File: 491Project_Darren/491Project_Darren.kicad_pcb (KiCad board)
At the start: 4 copper layers, 77 x 77 mm, 1 part, among them U2 Pico

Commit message: PCB
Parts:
- added C1: 100nF, 491_Footprints:CAP_805_CER, F.Cu at (142.5, 158.0)
- added C10: 100nF, 491_Footprints:CAP_805_CER, F.Cu at (148.5, 187.5)
- added C11: 10uF, 491_Footprints:CAP_ALUM, F.Cu at (127.0, 110.5)
- added C12: 10uF, 491_Footprints:CAP_ALUM, F.Cu at (154.0, 185.0)
- added C2: 100nF, 491_Footprints:CAP_805_CER, F.Cu at (124.5, 104.5)
- added C3: 10uF, 491_Footprints:CAP_ALUM, F.Cu at (154.9, 159.0)
- added C4: 0.1uF, 491_Footprints:CAP_CER_0.1uF_1206, F.Cu at (130.0, 194.0)
- added C5: 1000pF, 491_Footprints:CAP_805_CER, F.Cu at (129.9, 190.0)
- added C6: 1nF, 491_Footprints:CAP_805_CER, F.Cu at (129.9, 187.5)
- added C7: 22nF, 491_Footprints:CAP_805_CER, F.Cu at (129.5, 181.0)
- added C8: 100nF, 491_Footprints:CAP_805_CER, F.Cu at (139.5, 153.0)
- added C9: 100nF, 491_Footprints:CAP_805_CER, F.Cu at (119.9, 103.5)
- added J1: RJ45, 491_Footprints:RJ45_Amphenol_RJHSE5380, F.Cu at (116.0, 73.1)
- added J2: RJ45, 491_Footprints:RJ45_Amphenol_RJHSE5380, F.Cu at (175.3, 77.0)
- added R1: 110, 491_Footprints:R_805, F.Cu at (124.4, 88.5)
- added R10: 1k, 491_Footprints:R_805, F.Cu at (70.4, 89.8)
- added R11: 1k, 491_Footprints:R_805, F.Cu at (111.4, 153.0)
- added R12: 1k, 491_Footprints:R_805, F.Cu at (120.5, 96.5)
- added R13: 1k, 491_Footprints:R_805, F.Cu at (162.4, 159.0)
- added R14: 1k, 491_Footprints:R_805, F.Cu at (149.6, 164.0)
- added R15: 1k, 491_Footprints:R_805, F.Cu at (153.0, 191.6)
- added R16: 47k, 491_Footprints:R_805, F.Cu at (148.9, 192.0)
- added R17: 1k, 491_Footprints:R_805, F.Cu at (121.4, 109.0)
- added R18: 1k, 491_Footprints:R_805, F.Cu at (121.4, 107.0)
- added R19: 1k, 491_Footprints:R_805, F.Cu at (115.0, 99.0)
- added R2: 1k, 491_Footprints:R_805, F.Cu at (126.5, 93.0)
- added R20: 1k, 491_Footprints:R_805, F.Cu at (117.5, 99.0)
- added R21: 1k, 491_Footprints:R_805, F.Cu at (152.9, 195.0)
- added R22: 1k, 491_Footprints:R_805, F.Cu at (246.9, 128.5)
- added R3: 1k, 491_Footprints:R_805, F.Cu at (124.5, 93.0)
- added R4: 1k, 491_Footprints:R_805, F.Cu at (134.0, 99.0)
- added R5: 1k, 491_Footprints:R_805, F.Cu at (132.0, 99.0)
- added R6: 1k, 491_Footprints:R_805, F.Cu at (129.5, 104.0)
- added R7: 1k, 491_Footprints:R_805, F.Cu at (131.5, 104.0)
- added R8: 1k, 491_Footprints:R_805, F.Cu at (70.4, 85.5)
- added R9: 3k, 491_Footprints:R_805, F.Cu at (130.0, 184.0)
- added T1: ~, 491_Footprints:SM453230-181N7Y, F.Cu at (123.8, 84.5)
- added U1: ~, Package_SO:TSSOP-16_4.4x5mm_P0.65mm, F.Cu at (124.0, 99.0)
- added U3: ~, Package_SO:SOIC-28W_7.5x17.9mm_P1.27mm, F.Cu at (140.8, 186.6)
- U2: value Pico -> ~
- moved U2 95.5 mm to (217.9, 116.1)
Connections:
- U2 pad 1: (no net) -> SDA
- U2 pad 10: (no net) -> AES3-
- U2 pad 11: (no net) -> unconnected-(U2-GPIO8-Pad11)
- U2 pad 12: (no net) -> unconnected-(U2-GPIO9-Pad12)
- U2 pad 13: (no net) -> GND
- U2 pad 14: (no net) -> unconnected-(U2-GPIO10-Pad14)
- U2 pad 15: (no net) -> unconnected-(U2-GPIO11-Pad15)
- U2 pad 16: (no net) -> unconnected-(U2-GPIO12-Pad16)
- U2 pad 17: (no net) -> unconnected-(U2-GPIO13-Pad17)
- U2 pad 18: (no net) -> GND
- U2 pad 19: (no net) -> PWM
- U2 pad 2: (no net) -> SCL
- U2 pad 20: (no net) -> unconnected-(U2-GPIO15-Pad20)
- U2 pad 21: (no net) -> OLRCLK
- U2 pad 22: (no net) -> OSCLK
- U2 pad 23: (no net) -> GND
- U2 pad 24: (no net) -> SDOUT
- U2 pad 25: (no net) -> unconnected-(U2-GPIO19-Pad25)
- U2 pad 26: (no net) -> unconnected-(U2-GPIO20-Pad26)
- U2 pad 27: (no net) -> unconnected-(U2-GPIO21-Pad27)
- U2 pad 28: (no net) -> GND
- U2 pad 29: (no net) -> LED
- U2 pad 3: (no net) -> GND
- U2 pad 30: (no net) -> unconnected-(U2-RUN-Pad30)
- U2 pad 31: (no net) -> unconnected-(U2-GPIO26_ADC0-Pad31)
- U2 pad 32: (no net) -> unconnected-(U2-GPIO27_ADC1-Pad32)
- U2 pad 33: (no net) -> unconnected-(U2-AGND-Pad33)
- U2 pad 34: (no net) -> unconnected-(U2-GPIO28_ADC2-Pad34)
- U2 pad 35: (no net) -> unconnected-(U2-ADC_VREF-Pad35)
- U2 pad 36: (no net) -> +3V3
- U2 pad 37: (no net) -> unconnected-(U2-3V3_EN-Pad37)
- U2 pad 38: (no net) -> GND
- U2 pad 39: (no net) -> unconnected-(U2-VSYS-Pad39)
- U2 pad 4: (no net) -> RST
- U2 pad 40: (no net) -> unconnected-(U2-VBUS-Pad40)
- U2 pad 5: (no net) -> OMCLK
- U2 pad 6: (no net) -> RMCLK
- U2 pad 7: (no net) -> unconnected-(U2-GPIO5-Pad7)
- U2 pad 8: (no net) -> GND
- U2 pad 9: (no net) -> AES3+
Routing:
- net Net-(U1A-IN-): track 0.00 -> 15.7 mm, vias 0 -> 2
- net Net-(U1B-IN-): track 0.00 -> 15.5 mm
- net Net-(U1A-IN+): track 0.00 -> 12.7 mm
- net Net-(U1B-IN+): track 0.00 -> 12.7 mm
- net Net-(R1-Pad1): track 0.00 -> 12.5 mm
- net +3V3: track 0.00 -> 12.3 mm
- net SIG_IN+: track 0.00 -> 10.9 mm
- net AES3+: track 0.00 -> 9.77 mm
- net SIG_IN-: track 0.00 -> 8.41 mm
- net GND: track 0.00 -> 8.12 mm, vias 0 -> 2
- net AES3-: track 0.00 -> 8.07 mm
- net SIG_OUT+: track 0.00 -> 7.29 mm
- net Net-(R1-Pad2): track 0.00 -> 7.19 mm
- net SIG_OUT-: track 0.00 -> 2.50 mm
- net VCOM: track 0.00 -> 1.30 mm
- added copper zone on In2.Cu, net GND

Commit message: before lab push
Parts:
- moved R8 57.4 mm to (119.9, 114.5)
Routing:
- added copper zone on B.Cu, net GND
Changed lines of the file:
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@@
 		(tags "RJ45 8p8c ethernet cat5")
 		(property "Reference" "J1"
-			(at 3.56 -9.5 360)
+			(at 3.56 -9.5 0)
 			(layer "F.SilkS")
 			(effects
@@
 		)
 		(property "Value" "RJ45"
-			(at 3.56 9.5 360)
+			(at 3.56 9.5 0)
 			(layer "F.Fab")
 			(effects
@@
 		)
 		(fp_text user "${REFERENCE}"
-			(at 3.56 -6 360)
+			(at 3.56 -6 0)
 			(layer "F.Fab")
 			(effects
@@
 	(footprint "491_Footprints:R_805"
 		(layer "F.Cu")
-		(at 70.447201 85.5188)
+		(at 119.947201 114.5)
 		(property "Reference" "R8"
 			(at 0 -1.5 0)
@@
 			(polygon
 				(pts
-					(xy 70.273001 85.3196) (xy 70.621401 85.3196) (xy 70.621401 85.718) (xy 70.273001 85.718)
+					(xy 119.773001 114.3008) (xy 120.121401 114.3008) (xy 120.121401 114.6992) (xy 119.773001 114.6992)
 				)
 			)
@@
 			)
 		)
+	)
+	(zone
+		(net 14)
+		(net_name "GND")
+		(layer "B.Cu")
+		(hatch edge 0.5)
+		(connect_pads
+			(clearance 0.5)
+		)
+		(min_thickness 0.25)
+		(filled_areas_thickness no)
+		(fill
+			(thermal_gap 0.5)
+			(thermal_bridge_width 0.5)
+		)
+		(polygon
+			(pts
+				(xy 107 63) (xy 184 63) (xy 184 140) (xy 107.5 140)
+			)
+		)

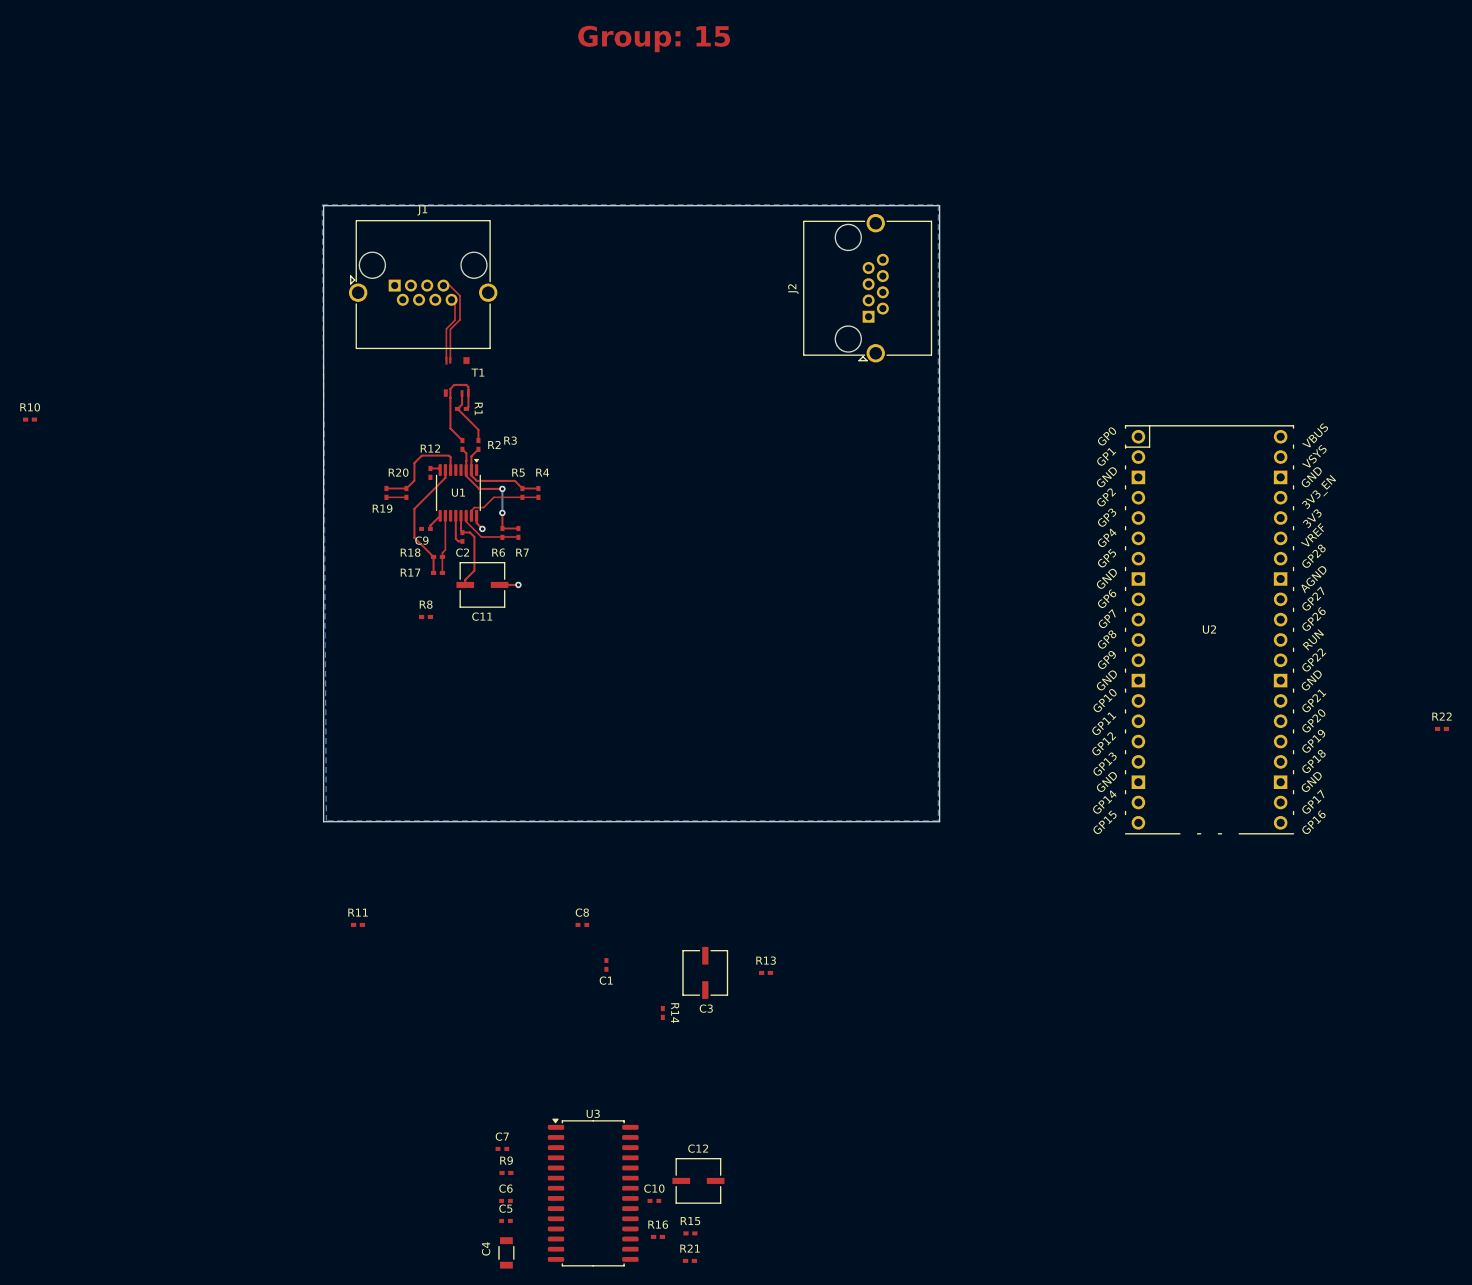
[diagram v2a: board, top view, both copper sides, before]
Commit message: Post lab
remember to keep differential pairs close together
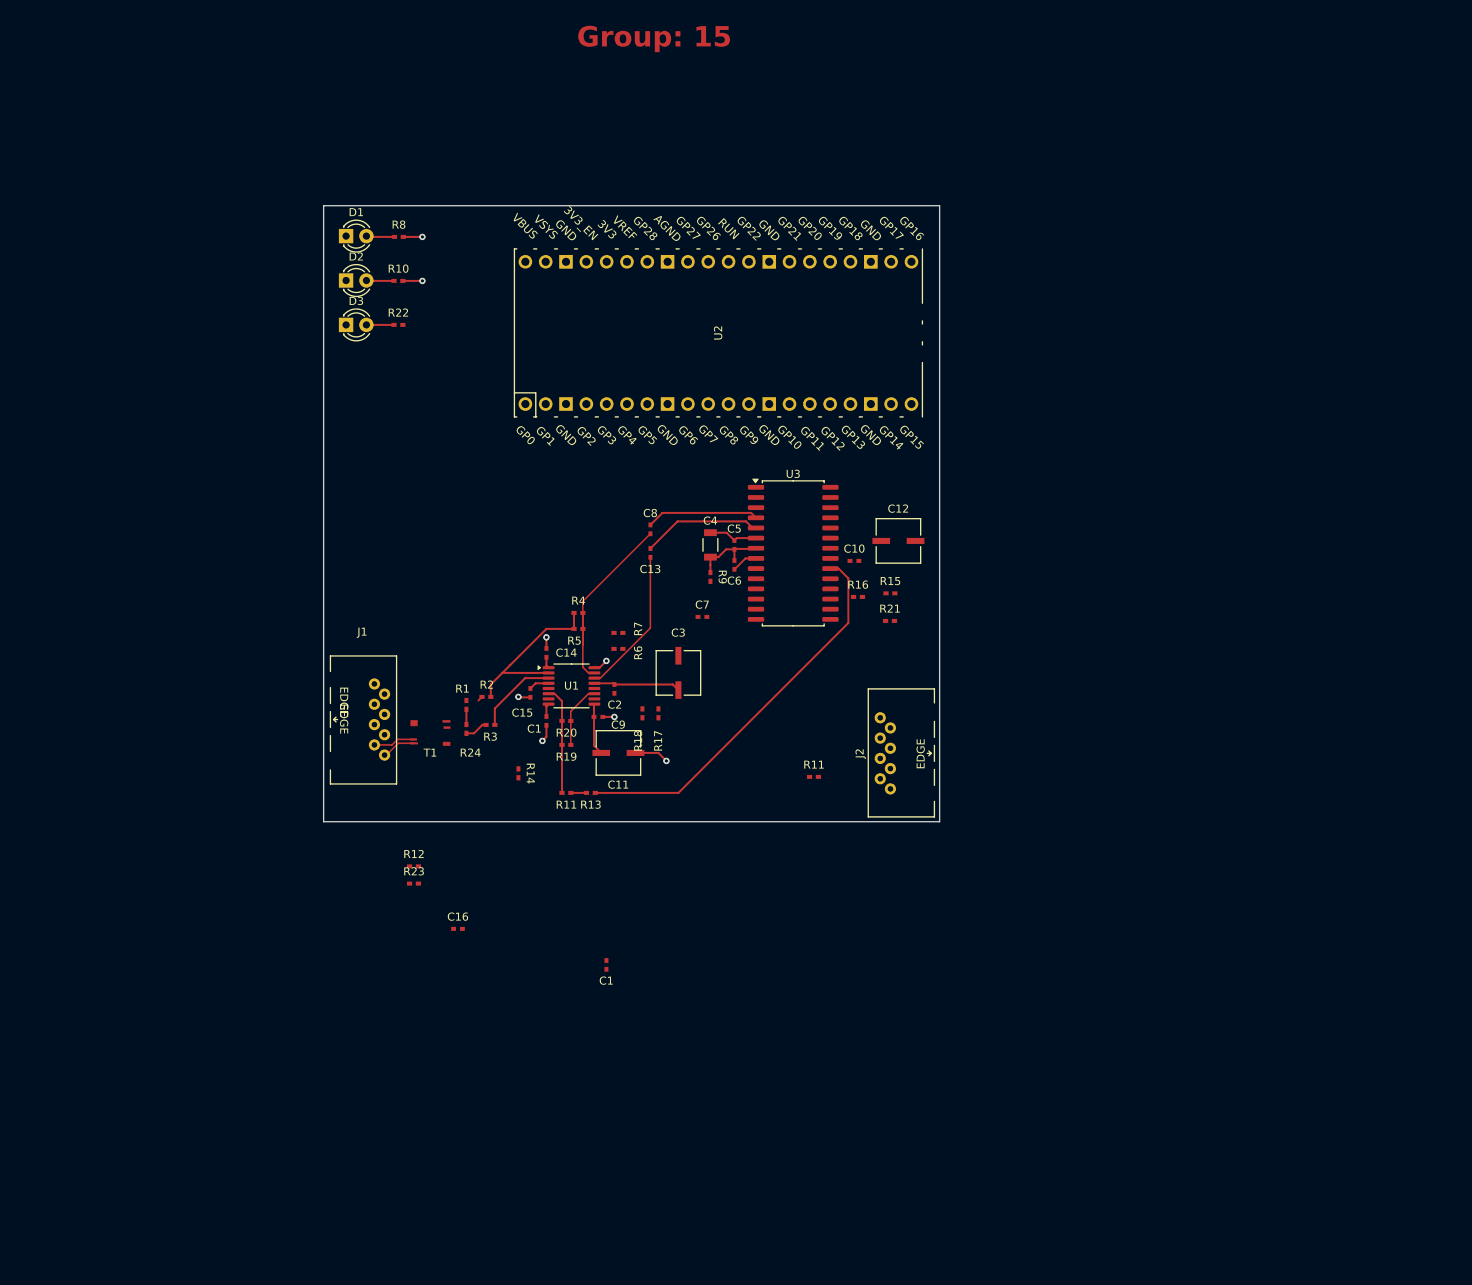
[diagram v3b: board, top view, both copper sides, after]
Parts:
- added C1: 100nF, 491_Footprints:CAP_805_CER, F.Cu at (135.0, 127.5)
- added C13: 10nF, 491_Footprints:CAP_805_CER, F.Cu at (148.0, 106.5)
- added C14: 100nF, 491_Footprints:CAP_805_CER, F.Cu at (135.0, 119.0)
- added C15: 100nF, 491_Footprints:CAP_805_CER, F.Cu at (133.0, 124.0)
- added C16: 100nF, 491_Footprints:CAP_805_CER, F.Cu at (123.9, 153.5)
- added D1: RED, LED_THT:LED_D3.0mm, F.Cu at (110.0, 66.9)
- added D2: RED, LED_THT:LED_D3.0mm, F.Cu at (110.0, 72.5)
- added D3: RED, LED_THT:LED_D3.0mm, F.Cu at (110.0, 78.0)
- added R11: 100, 491_Footprints:R_805, F.Cu at (137.5, 136.5)
- added R23: 50, 491_Footprints:R_805, F.Cu at (118.4, 147.8)
- added R24: 52, 491_Footprints:R_805, F.Cu at (125.0, 128.5)
- C8: value 100nF -> 10nF
- J1, J2: footprint 491_Footprints:RJ45_Amphenol_RJHSE5380 -> 491_Footprints:RJ45_Conn
- R1: value 110 -> 52
- R12: value 1k -> 50
- R13: value 1k -> 900
- moved R22 139.9 mm to (116.5, 78.0), turned to 180 degrees
- moved C4 92.1 mm to (155.5, 105.5), turned to -90 degrees
- moved C5 89.2 mm to (158.5, 105.5), turned to -90 degrees
- moved C6 84.5 mm to (158.5, 108.0), turned to 90 degrees
- moved C10 83.8 mm to (173.5, 107.5)
- moved C12 83.8 mm to (179.0, 105.0)
- moved R15 83.8 mm to (178.0, 111.6)
- moved R16 83.8 mm to (173.9, 112.0)
- moved R21 83.8 mm to (177.9, 115.0)
- moved U3 83.8 mm to (165.8, 106.6)
- moved R9 78.7 mm to (155.5, 109.5), turned to -90 degrees
- moved U2 71.7 mm to (156.5, 79.0), turned to 90 degrees
- moved C7 71.0 mm to (154.5, 114.5)
- moved R11 59.9 mm to (168.4, 134.5)
- moved J2 54.6 mm to (178.0, 131.6)
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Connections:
- C10 pad 1: +3V3 -> +5V
- C10 pad 2: Net-(C10-Pad2) -> GND
- C11 pad 1: +3V3 -> +5V
- C12 pad 1: +3V3 -> +5V
- C12 pad 2: Net-(C10-Pad2) -> GND
- C2 pad 1: +3V3 -> +5V
- C3 pad 1: +3V3 -> +5V
- C8 pad 1: VCOM -> AES3+
- C8 pad 2: GND -> Net-(U3-RXP0)
- C9 pad 1: +3V3 -> +5V
- R10 pad 1: +5VA -> +5V
- R12 pad 1: VCOM -> Net-(U1B-OUT-)
- R12 pad 2: GND -> SIG_OUT-
- R13 pad 2: Net-(U1B-IN+) -> Net-(R11-Pad1)
- R15 pad 2: +3V3 -> +5V
- R16 pad 2: +3V3 -> +5V
- R17 pad 2: SIG_OUT+ -> Net-(U1B-OUT+)
- R18 pad 2: SIG_OUT+ -> Net-(U1B-OUT+)
- R19 pad 2: SIG_OUT- -> Net-(U1B-OUT-)
- R20 pad 2: SIG_OUT- -> Net-(U1B-OUT-)
- R21 pad 2: +3V3 -> +5V
- R3 pad 1: Net-(R1-Pad1) -> Net-(R24-Pad1)
- R5 pad 1: Net-(U1A-IN+) -> AES3+
- R5 pad 2: AES3+ -> Net-(U1A-IN+)
- R8 pad 1: +3V3 -> +5V
- T1 pad 7: Net-(R1-Pad1) -> Net-(R24-Pad1)
- U1 pad 1: unconnected-(U1A-~{PD}-Pad1) -> Net-(U1A-~{PD})
- U1 pad 10: SIG_OUT+ -> Net-(U1B-OUT+)
- U1 pad 11: SIG_OUT- -> Net-(U1B-OUT-)
- U1 pad 13: +3V3 -> +5V
- U1 pad 4: VCOM -> Net-(U1A-VOCM)
- U1 pad 8: VCOM -> Net-(U1B-VOCM)
- U1 pad 9: +3V3 -> +5V
- U2 pad 36: +3V3 -> VA
- U2 pad 40: unconnected-(U2-VBUS-Pad40) -> +5V
- U3 pad 21: +3V3 -> +5V
- U3 pad 23: +3V3 -> +5V
- U3 pad 4: AES+ -> Net-(U3-RXP0)
- U3 pad 5: AES- -> Net-(U3-RXN)
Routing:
- net PASS+: track 0.00 -> 48.8 mm
- net +5V: track 0.00 -> 22.2 mm, vias 0 -> 2
- net AES3+: track 9.77 -> 25.9 mm
- net Net-(U1B-IN-): track 15.5 -> 0.00 mm
- net Net-(U3-RXN): track 0.00 -> 14.9 mm
- net Net-(U3-RXP0): track 0.00 -> 14.1 mm
- net +3V3: track 12.3 -> 0.00 mm
- net Net-(R1-Pad1): track 12.5 -> 1.89 mm
- net AES3-: track 8.07 -> 18.4 mm
- net Net-(U1A-IN+): track 12.7 -> 22.6 mm
- net GNDA: track 0.00 -> 9.47 mm
- net Net-(U1B-OUT-): track 0.00 -> 8.05 mm
- net SIG_OUT+: track 7.29 -> 0.00 mm
- net Net-(R1-Pad2): track 7.19 -> 0.63 mm
- net VA: track 0.00 -> 6.26 mm
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- added copper zone on In2.Cu, net +5V
- added copper zone on In1.Cu, net GND
- removed copper zone on B.Cu, net GND
- removed copper zone on In2.Cu, net GND
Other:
- board text added: "EDGE"
